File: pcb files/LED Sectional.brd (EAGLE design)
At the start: 69.8 x 36.8 mm, 9 parts, among them IC1 74HCT245N, J1 POWER_JACK

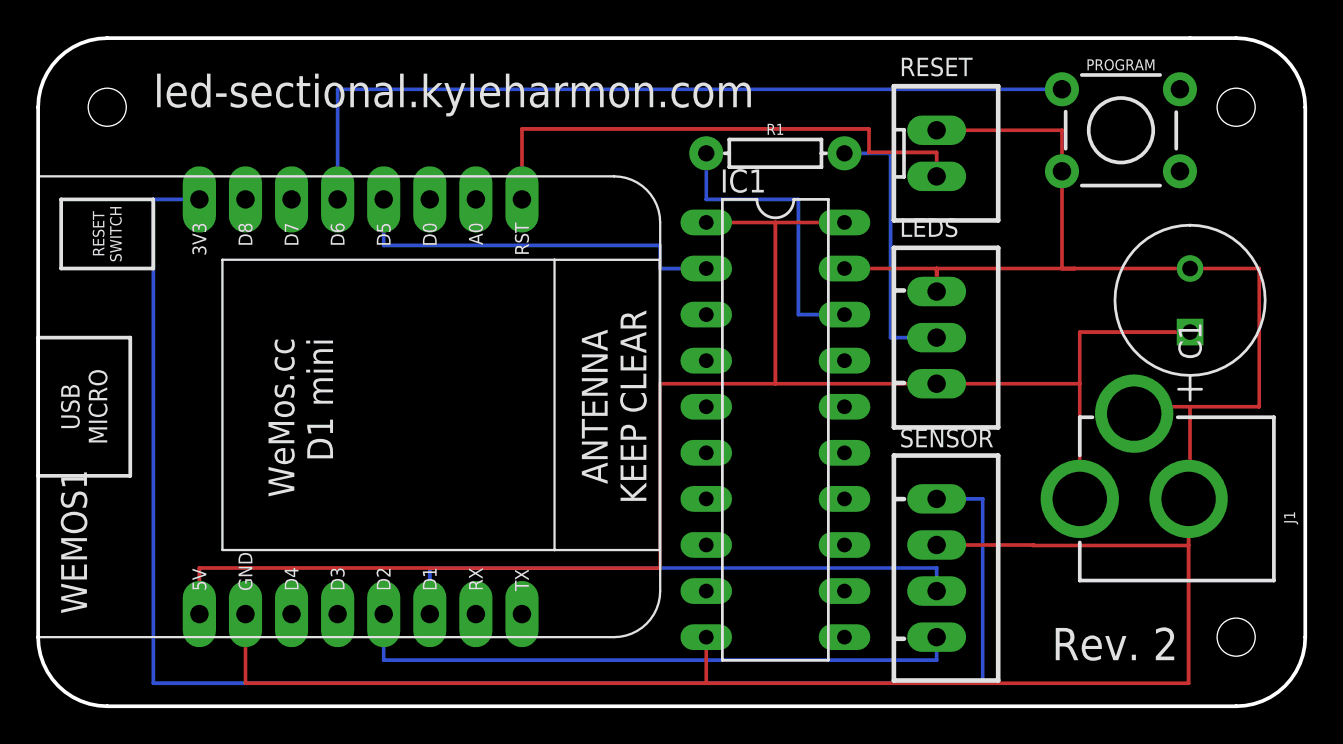
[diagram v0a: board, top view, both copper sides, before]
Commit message: Update default pin; update pcb layout.
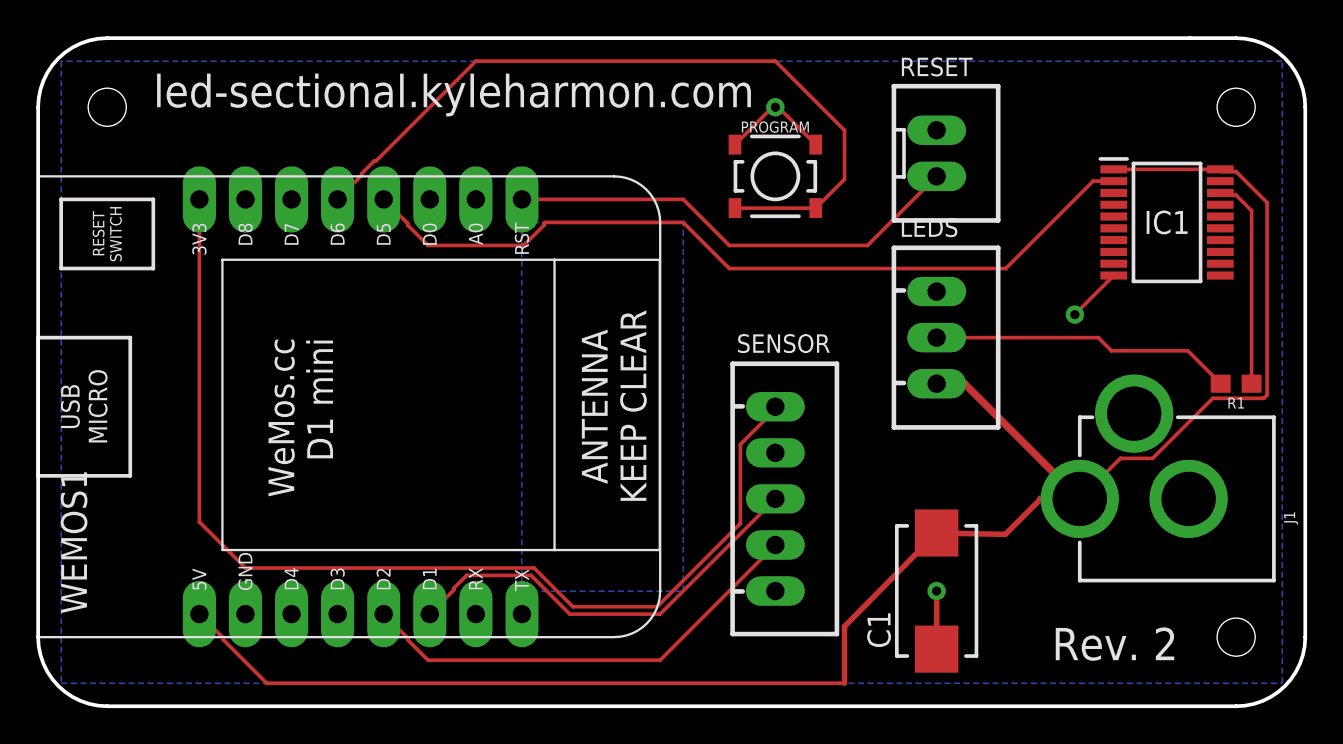
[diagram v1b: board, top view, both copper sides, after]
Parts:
- C1: value RL80J102MDN1KX -> 1000uF; device Kyle's Custom:RL8 -> adafruit:CT7343
- IC1: value 74HCT245N -> SN74HCT245PW; device 74xx-eu:DIL20 -> SN74HCT245PW:SOP65P640X120-20N
- PROGRAM: value MOMENTARY-SWITCH-SPST-PTH-6.0MM -> MOMENTARY-SWITCH-SPST-SMD-4.5MM; device SparkFun-Switches:TACTILE_SWITCH_PTH_6.0MM -> SparkFun-Switches:TACTILE_SWITCH_SMD_4.5MM
- R1: device SparkFun-Resistors:AXIAL-0.3 -> SparkFun-Resistors:0603
- SENSOR: value JST-XH-04-PIN-LONG-PAD -> JST-XH-05-PIN-LONG-PAD; device Rembrandt Electronics - JST XH Connectors v1-0:JST-XH-04-PACKAGE-LONG-PAD -> Rembrandt Electronics - JST XH Connectors v1-0:JST-XH-05-PACKAGE-LONG-PAD
- moved R1 28.4 mm to (66.0, 17.8), turned to 180 degrees
- moved IC1 24.4 mm to (62.2, 26.7), turned to 0 degrees
- moved C1 22.6 mm to (49.5, 6.35)
- moved PROGRAM 19.2 mm to (40.6, 29.2)
- moved SENSOR 9.67 mm to (40.6, 11.4)
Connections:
- net GND: now also C1.-, PROGRAM.1, PROGRAM.4; no longer C1.2, IC1.19, PROGRAM.3
- net N$2: now also R1.2; no longer R1.P$2
- net N$4: now also R1.1; no longer R1.P$1
- net N$7: now also PROGRAM.2, PROGRAM.3; no longer PROGRAM.1
- net VCC: now also C1.+; no longer C1.1
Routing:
- net GND: track 142.8 -> 12.4 mm, vias 0 -> 3
- net N$1: track 87.6 -> 58.7 mm
- net N$3: track 21.6 -> 45.0 mm
- net N$6: track 34.3 -> 25.3 mm
- net N$5: track 31.8 -> 23.5 mm
- net VCC: track 93.0 -> 99.3 mm
- net N$4: track 16.5 -> 11.7 mm
- net N$8: track 29.4 -> 25.5 mm
- net N$7: track 46.0 -> 42.1 mm
- net N$2: track 15.2 -> 16.7 mm
- added copper zone on layer 16, net GND
